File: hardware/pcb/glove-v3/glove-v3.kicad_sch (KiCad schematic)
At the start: 18 parts, among them U1 XIAO-ESP32C3, U2 CD74HC4067M96

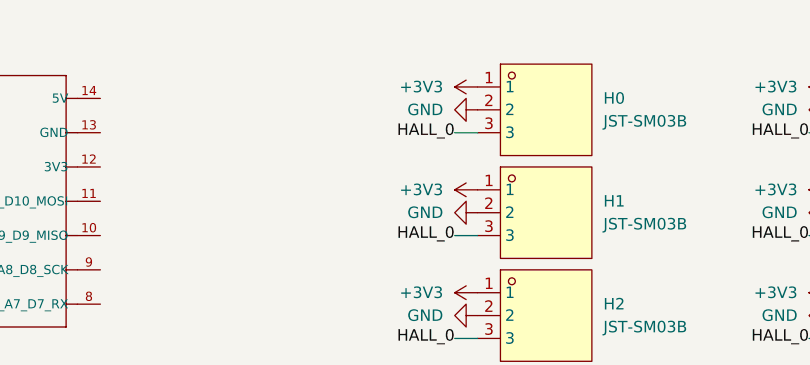
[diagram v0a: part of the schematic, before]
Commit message: added decoupling capacitor and updated footprints
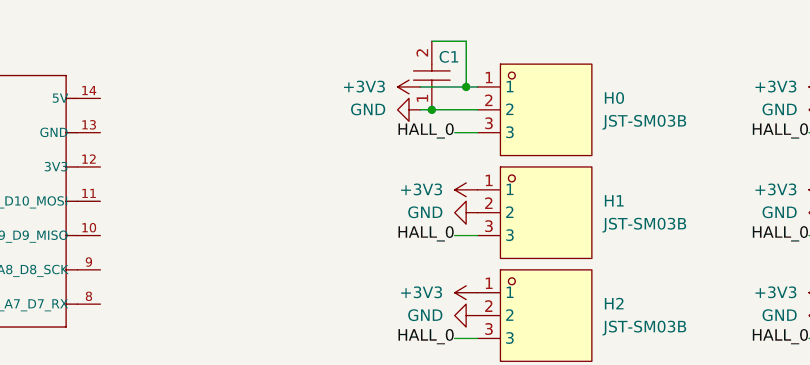
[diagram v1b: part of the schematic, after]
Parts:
- added C1: C-0402-0.01uF, 0_easyeda2kicad:C0402, symbol 0_easyeda2kicad:C-0402-0.01uF
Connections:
- net +3V3: now also C1.2
- net GND: now also C1.1
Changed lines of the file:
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@@
 	(generator_version "8.0")
 	(paper "A4")
+	(junction
+		(at 135.89 30.48)
+		(diameter 0)
+		(color 0 0 0 0)
+	)
+	(junction
+		(at 132.08 33.02)
+		(diameter 0)
+		(color 0 0 0 0)
+	)
 	(wire
 		(pts
@@
 	(wire
 		(pts
-			(xy 173.99 69.85) (xy 176.53 69.85)
+			(xy 135.89 30.48) (xy 137.16 30.48)
 		)
 		(stroke
@@
 	(wire
 		(pts
-			(xy 173.99 92.71) (xy 176.53 92.71)
+			(xy 173.99 69.85) (xy 176.53 69.85)
 		)
 		(stroke
@@
 	(wire
 		(pts
-			(xy 173.99 58.42) (xy 176.53 58.42)
+			(xy 132.08 33.02) (xy 137.16 33.02)
 		)
 		(stroke
@@
 	(wire
 		(pts
-			(xy 173.99 81.28) (xy 176.53 81.28)
+			(xy 132.08 25.4) (xy 135.89 25.4)
 		)
 		(stroke
@@
 	(wire
 		(pts
-			(xy 134.62 46.99) (xy 137.16 46.99)
+			(xy 173.99 92.71) (xy 176.53 92.71)
 		)
 		(stroke
@@
 	(wire
 		(pts
-			(xy 134.62 92.71) (xy 137.16 92.71)
+			(xy 173.99 58.42) (xy 176.53 58.42)
 		)
 		(stroke
@@
 	(wire
 		(pts
-			(xy 134.62 81.28) (xy 137.16 81.28)
+			(xy 173.99 81.28) (xy 176.53 81.28)
 		)
 		(stroke
@@
 	(wire
 		(pts
-			(xy 134.62 104.14) (xy 137.16 104.14)
+			(xy 134.62 46.99) (xy 137.16 46.99)
 		)
 		(stroke
@@
 	(wire
 		(pts
-			(xy 173.99 35.56) (xy 176.53 35.56)
+			(xy 134.62 92.71) (xy 137.16 92.71)
 		)
 		(stroke
@@
 	(wire
 		(pts
-			(xy 173.99 104.14) (xy 176.53 104.14)
+			(xy 134.62 81.28) (xy 137.16 81.28)
 		)
 		(stroke
@@
 	(wire
 		(pts
-			(xy 134.62 69.85) (xy 137.16 69.85)
+			(xy 134.62 104.14) (xy 137.16 104.14)
 		)
 		(stroke
@@
 	(wire
 		(pts
-			(xy 173.99 46.99) (xy 176.53 46.99)
+			(xy 173.99 35.56) (xy 176.53 35.56)
 		)
 		(stroke
@@
 	(wire
 		(pts
-			(xy 134.62 58.42) (xy 137.16 58.42)
+			(xy 173.99 104.14) (xy 176.53 104.14)
 		)
 		(stroke
@@
 	(wire
 		(pts
-			(xy 173.99 115.57) (xy 176.53 115.57)
+			(xy 134.62 69.85) (xy 137.16 69.85)
 		)
 		(stroke
@@
 	(wire
 		(pts
-			(xy 134.62 35.56) (xy 137.16 35.56)
+			(xy 135.89 25.4) (xy 135.89 30.48)
 		)
 		(stroke
@@
 		)
 	)
+	(wire
+		(pts
+			(xy 173.99 46.99) (xy 176.53 46.99)
+		)
+		(stroke
+			(width 0)
+			(type default)
+		)
+	)
+	(wire
+		(pts
+			(xy 134.62 58.42) (xy 137.16 58.42)
+		)
+		(stroke
+			(width 0)
+			(type default)
+		)
+	)
+	(wire
+		(pts
+			(xy 130.81 33.02) (xy 132.08 33.02)
+		)
+		(stroke
+			(width 0)
+			(type default)
+		)
+	)
+	(wire
+		(pts
+			(xy 130.81 30.48) (xy 135.89 30.48)
+		)
+		(stroke
+			(width 0)
+			(type default)
+		)
+	)
+	(wire
+		(pts
+			(xy 173.99 115.57) (xy 176.53 115.57)
+		)
+		(stroke
+			(width 0)
+			(type default)
+		)
+	)
+	(wire
+		(pts
+			(xy 134.62 35.56) (xy 137.16 35.56)
+		)
+		(stroke
+			(width 0)
+			(type default)
+		)
+	)
 	(label "HALL_0"
 		(at 173.99 104.14 180)
@@
 	(symbol
 		(lib_id "power:GND")
-		(at 137.16 33.02 270)
+		(at 130.81 33.02 270)
 		(unit 1)
 		(exclude_from_sim no)
@@
 		(fields_autoplaced yes)
 		(property "Reference" "#PWR01"
+			(at 124.46 33.02 0)
+			(effects
+				(font
+					(size 1.27 1.27)
+				)
+				(hide yes)
+			)
+		)
+		(property "Value" "GND"
+			(at 127 33.0199 90)
+			(effects
+				(font
+					(size 1.27 1.27)
+				)
+				(justify right)
+			)
+		)
+		(property "Footprint" ""
 			(at 130.81 33.02 0)
 			(effects
@@
 			)
 		)
-		(property "Value" "GND"
-			(at 133.35 33.0199 90)
-			(effects
-				(font
-					(size 1.27 1.27)
-				)
-				(justify right)
-			)
-		)
-		(property "Footprint" ""
-			(at 137.16 33.02 0)
-			(effects
-				(font
-					(size 1.27 1.27)
-				)
-				(hide yes)
-			)
-		)
 		(property "Datasheet" ""
-			(at 137.16 33.02 0)
+			(at 130.81 33.02 0)
 			(effects
 				(font
@@
 		)
 		(property "Description" "Power symbol creates a global label with name \"GND\" , ground"
-			(at 137.16 33.02 0)
+			(at 130.81 33.02 0)
 			(effects
 				(font
@@
 	)
 	(symbol
+		(lib_id "0_easyeda2kicad:C-0402-0.01uF")
+		(at 132.08 29.21 90)
+		(unit 1)
+		(exclude_from_sim no)
+		(in_bom yes)
+		(on_board yes)
+		(dnp no)
+		(property "Reference" "C1"
+			(at 132.842 27.178 90)
+			(effects
+				(font
+					(size 1.27 1.27)
+				)
+				(justify right)
+			)
+		)
+		(property "Value" "C-0402-0.01uF"
+			(at 137.16 29.21 0)
+			(effects
+				(font
+					(size 1.27 1.27)
+				)
+				(hide yes)
+			)
+		)
+		(property "Footprint" "0_easyeda2kicad:C0402"
+			(at 139.7 29.21 0)
+			(effects
+				(font
+					(size 1.27 1.27)
+				)
+				(hide yes)
+			)
+		)
+		(property "Datasheet" "https://lcsc.com/product-detail/Multilayer-Ceramic-Capacitors-MLCC-SMD-SMT_SAMSUNG_CL05B103KB5NNNC_10nF-103-10-50V_C15195.html"
+			(at 142.24 29.21 0)
+			(effects
+				(font
+					(size 1.27 1.27)
+				)
+				(hide yes)
+			)
+		)
+		(property "Description" ""
+			(at 132.08 29.21 0)
+			(effects
+				(font
+					(size 1.27 1.27)
+				)
+				(hide yes)
+			)
+		)
+		(property "LCSC Part" "C15195"
+			(at 144.78 29.21 0)
+			(effects
+				(font
+					(size 1.27 1.27)
+				)
+				(hide yes)
+			)
+		)
+		(pin "1"
+		)
+		(pin "2"
+		)
+		(instances
+			(project "glove-v3"
+				(path "/29a0f5b3-0112-40bd-a6f2-14aa548dfb77"
+					(reference "C1")
+					(unit 1)
+				)
+			)
+		)
+	)
+	(symbol
 		(lib_id "0_easyeda2kicad:SM03B-SRSS-TB(LF)(SN)(P)")
 		(at 181.61 33.02 0)
@@
 	(symbol
 		(lib_id "power:+3V3")
-		(at 137.16 30.48 90)
-		(unit 1)
-		(exclude_from_sim no)
-		(in_bom yes)
-		(on_board yes)
-		(dnp no)
-		(fields_autoplaced yes)
+		(at 130.81 30.48 90)
+		(unit 1)
+		(exclude_from_sim no)
+		(in_bom yes)
+		(on_board yes)
+		(dnp no)
 		(property "Reference" "#PWR02"
-			(at 140.97 30.48 0)
+			(at 134.62 30.48 0)
 			(effects
 				(font
@@
 		)
 		(property "Value" "+3V3"
-			(at 133.35 30.4799 90)
+			(at 127 30.4799 90)
 			(effects
 				(font
@@
 		)
 		(property "Footprint" ""
-			(at 137.16 30.48 0)
+			(at 130.81 30.48 0)
 			(effects
 				(font
@@
 		)
 		(property "Datasheet" ""
-			(at 137.16 30.48 0)
+			(at 130.81 30.48 0)
 			(effects
 				(font
@@
 		)
 		(property "Description" "Power symbol creates a global label with name \"+3V3\""
-			(at 137.16 30.48 0)
-			(effects
-				(font
+			(at 130.81 30.48 0)
+			(effects
+				(font

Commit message: schematic done and board layout done
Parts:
- removed H15: JST-SM03B, 0_easyeda2kicad:CONN-SMD_SM03B-SRSS-TB-LF-SN-P, symbol 0_easyeda2kicad:SM03B-SRSS-TB(LF)(SN)(P)
- added C0, C1, C10, C11, C12, C13, C14, C2, C3, C4, C5, C6, C7, C8, C9: C-0402-0.01uF, 0_easyeda2kicad:C0402, symbol 0_easyeda2kicad:C-0402-0.01uF
- added H0: JST-SM03B, 0_easyeda2kicad:CONN-SMD_SM03B-SRSS-TB-LF-SN-P, symbol 0_easyeda2kicad:SM03B-SRSS-TB(LF)(SN)(P)
- renumbered C1 to C15, H0 to H15
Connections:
- net +3V3: now also H1.3, H10.3, H11.3, H12.3, H13.3, H14.3, H15.3, H2.3, H3.3, H4.3, H5.3, H6.3, H7.3, H8.3, H9.3, U1.12 (3V3), U2.24 (VCC), C0.2, C1.2, C10.2, C11.2, C12.2, C13.2, C14.2, C2.2, C3.2, C4.2, C5.2, C6.2, C7.2, C8.2, C9.2, H0.3; no longer H1.1, H10.1, H11.1, H12.1, H13.1, H14.1, H15.1, H2.1, H3.1, H4.1, H5.1, H6.1, H7.1, H8.1, H9.1
- net GND: now also U1.13 (GND), U2.12 (GND), U2.15 (~{E}), C0.1, C1.1, C10.1, C11.1, C12.1, C13.1, C14.1, C2.1, C3.1, C4.1, C5.1, C6.1, C7.1, C8.1, C9.1, H0.2
- net HALL_0: now also U2.9 (I0), H0.1; no longer H1.3, H10.3, H11.3, H12.3, H13.3, H14.3, H15.3, H2.3, H3.3, H4.3, H5.3, H6.3, H7.3, H8.3, H9.3
- net S0: now reaches U1.10 (PA5_A9_D9_MISO)
- net S0: now also U2.10 (S0)
- net MUX_OUT: now reaches U1.3 (PA10_A2_D2)
- net MUX_OUT: now also U2.1 (COMMONINPUT/OUTPUT)
- net S2: now reaches U1.5 (PA8_A4_D4_SDA)
- net S2: now also U2.14 (S2)
- net S3: now reaches U1.6 (PA9_A5_D5_SCL)
- net S3: now also U2.13 (S3)
- net S1: now reaches U1.9 (PA7_A8_D8_SCK)
- net S1: now also U2.11 (S1)
- net HALL_15: now reaches U2.16 (I15)
- net HALL_15: now also H15.1
- net HALL_14: now reaches U2.17 (I14)
- net HALL_14: now also H14.1
- net HALL_13: now reaches U2.18 (I13)
- net HALL_13: now also H13.1
- net HALL_12: now reaches U2.19 (I12)
- net HALL_12: now also H12.1
- net HALL_7: now reaches U2.2 (I7)
- net HALL_7: now also H7.1
- net HALL_11: now reaches U2.20 (I11)
- net HALL_11: now also H11.1
- net HALL_10: now reaches U2.21 (I10)
- net HALL_10: now also H10.1
- net HALL_9: now reaches U2.22 (I9)
- net HALL_9: now also H9.1
- net HALL_8: now reaches U2.23 (I8)
- net HALL_8: now also H8.1
- net HALL_6: now reaches U2.3 (I6)
- net HALL_6: now also H6.1
- net HALL_5: now reaches U2.4 (I5)
- net HALL_5: now also H5.1
- net HALL_4: now reaches U2.5 (I4)
- net HALL_4: now also H4.1
- net HALL_3: now reaches U2.6 (I3)
- net HALL_3: now also H3.1
- net HALL_2: now reaches U2.7 (I2)
- net HALL_2: now also H2.1
- net HALL_1: now reaches U2.8 (I1)
- net HALL_1: now also H1.1
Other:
- moved on the sheet: C15, H15

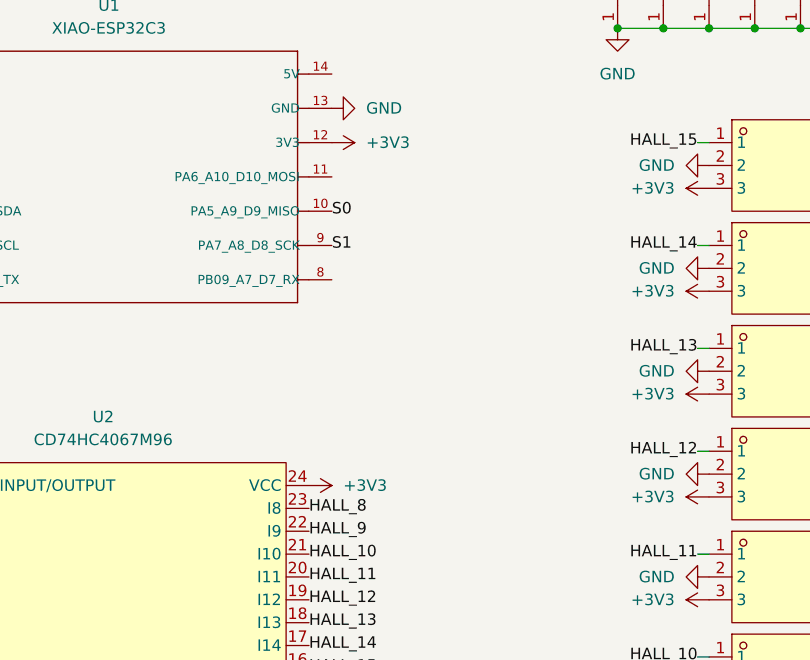
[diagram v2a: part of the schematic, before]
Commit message: glove-v3.0 done and ordered on JLCPCB
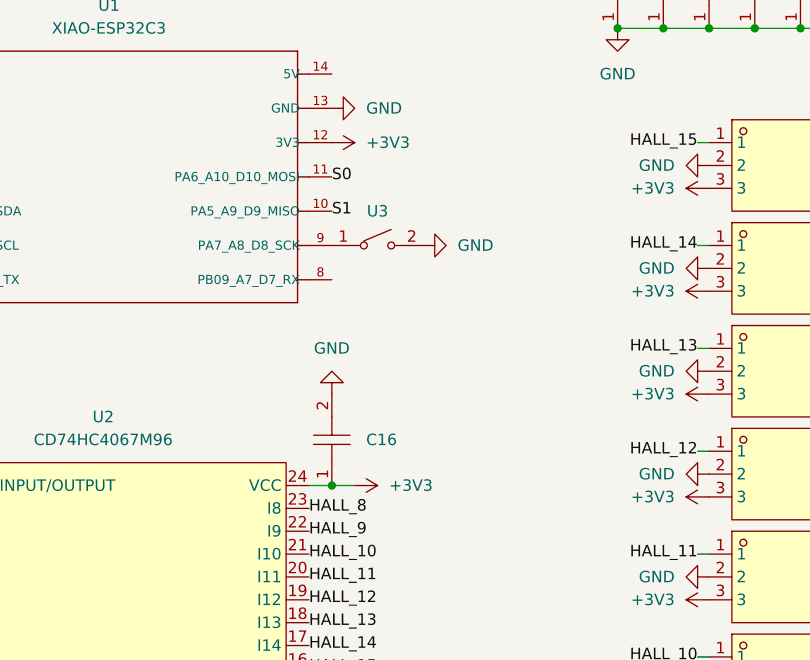
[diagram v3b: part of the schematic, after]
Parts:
- added C16: C-0402-0.1uF, 0_easyeda2kicad:C0402, symbol 0_easyeda2kicad:C-0402-0.1uF
- added U3: 2.5x3mm-BUTTON, 0_easyeda2kicad:KEY-SMD_L3.0-W2.5-LS4.0_TD-1183SN, symbol 0_easyeda2kicad:2.5x3mm-BUTTON
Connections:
- net +3V3: now also C16.1
- net GND: now also C16.2, U3.2
- net S0: now also U1.11 (PA6_A10_D10_MOSI); no longer U1.10 (PA5_A9_D9_MISO)
- net S1: now also U1.10 (PA5_A9_D9_MISO); no longer U1.9 (PA7_A8_D8_SCK)
- new net: U1.9 (PA7_A8_D8_SCK), U3.1
